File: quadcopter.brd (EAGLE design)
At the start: 196 x 196 mm, 65 parts, among them J1 ISP, U1 ATMEGA128RFA1

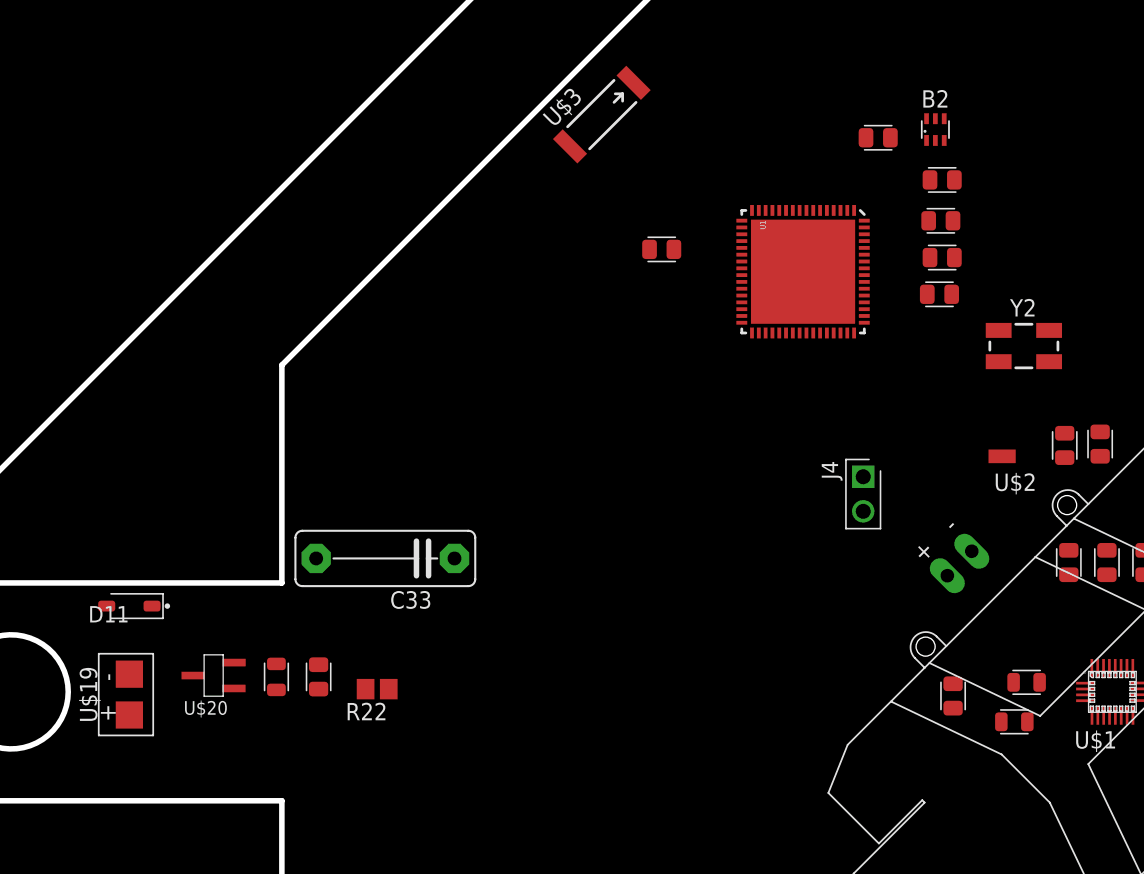
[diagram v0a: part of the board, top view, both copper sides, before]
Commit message: figured out pour, finished the gnd layer. need to continue from 3v and vbat pours
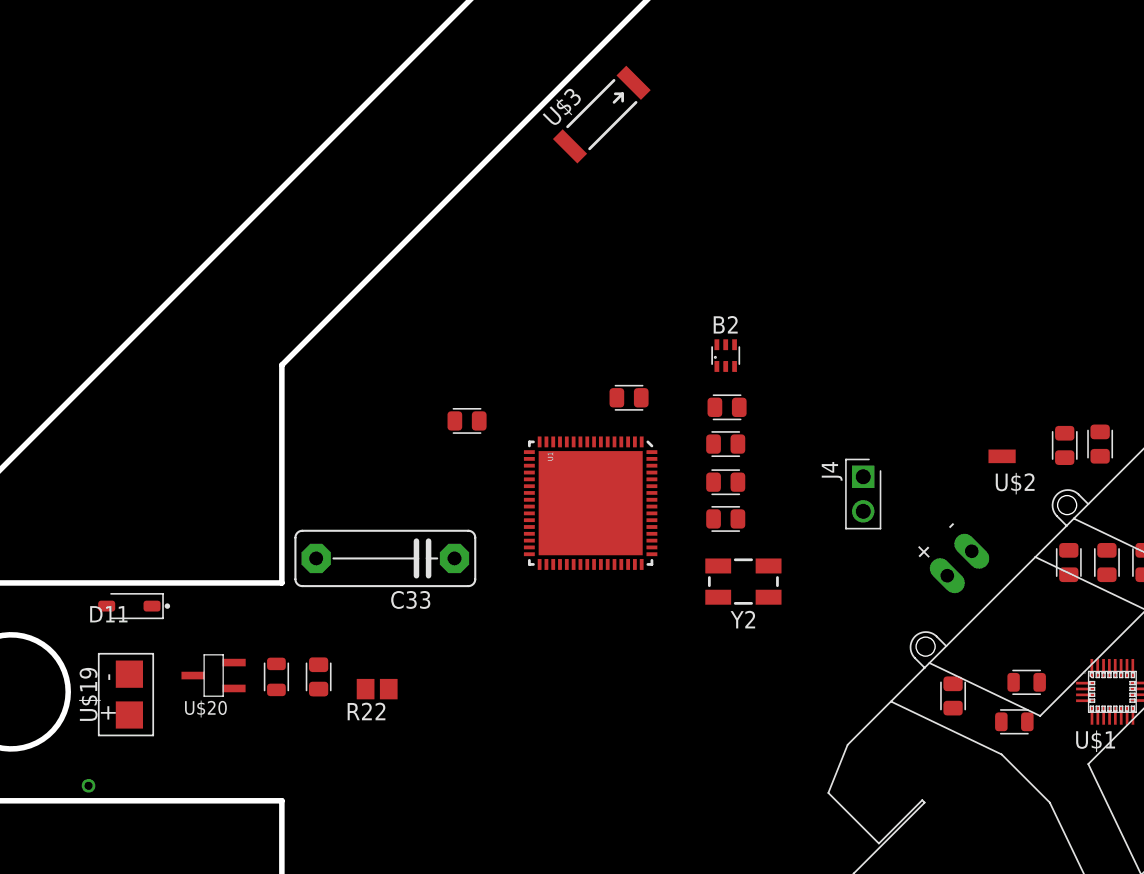
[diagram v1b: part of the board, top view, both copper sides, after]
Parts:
- moved Y2 26.9 mm to (-27.1, 8.10), turned to 180 degrees
- moved C8 26.5 mm to (-35.5, 21.6)
- moved U1 23.1 mm to (-38.3, 13.9)
- moved C7 23.0 mm to (-28.3, 20.9)
- moved C2 22.9 mm to (-28.4, 15.4)
- moved C1 22.8 mm to (-28.4, 12.7)
- moved C6 22.8 mm to (-28.4, 18.2)
- moved B2 22.6 mm to (-28.4, 24.7)
- moved C5 19.1 mm to (-47.4, 19.9)
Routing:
- added copper zone on layer 15, net GND
